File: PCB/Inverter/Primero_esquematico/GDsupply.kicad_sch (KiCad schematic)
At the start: 43 parts, among them T1 750317595, U1 UCC21750QDWRQ1, U2 LM25180QNGURQ1

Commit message: Correcciones incompletas e instalaciones de un par de extensiones copadas
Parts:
- removed C2, C3: 10uF, symbol Device:C
- removed C4: 47nF, symbol Device:C
- removed D1: 1N4148WS-Q, Diode_SMD:D_SOD-323F, symbol Device:D
- removed D2: DFLZ24Q-7, symbol Device:D_Zener
- removed D3, D41: VS-10MQ100NTRPBF, symbol Device:D_Schottky
- removed D5: BZT52C18-7-F, symbol Device:D_Zener
- removed D6: BZT52-B8V2_R1_00001, symbol Device:D_Zener
- removed R1: 307k, symbol Device:R
- removed R2: 37k, symbol Device:R
- removed R3: 12k1, symbol Device:R
- removed R4: 200k, symbol Device:R
- removed R5: 154k, symbol Device:R
- removed T1: 750317595, FSAE-footprints:WE-FLYTI_EP7_4436, symbol Fsae:750317595
- removed U2: LM25180QNGURQ1, NGU0008C, symbol Fsae:LM25180QNGURQ1
- added C2: EEH-ZS1H271UP, Capacitor_SMD:CP_Elec_10x10, symbol Device:C_Polarized_Small_US
- added D1: SMDJ13A, Diode_SMD:D_SMC, symbol Device:D_TVS
- added J1: IHL0212D1509, Snapeda:CONN5_05D1509_XPR, symbol Snapeda:IHL0205D1509
- added L1: MLZ2012N6R8LT000, Inductor_SMD:L_0805_2012Metric, symbol Device:L
- C1: value 10uF -> CL31B475KAHNNNE; footprint (none) -> Capacitor_SMD:C_1206_3216Metric; Compra (none) -> https://www.digikey.com/en/products/detail/samsung-electro-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
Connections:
- net +15V: now also J1.7 (+Vout)
- net -8V: now also J1.5 (-Vout)
- net GND: now also C1.2, C2.2, D1.2 (A2), J1.2 (-Vin); no longer C1.1
- net ISO_GND: now also J1.6 (Common)
- net Vin_FB: now also L1.1; no longer C1.2
- new net: C1.1, C2.1, D1.1 (A1), J1.1 (+Vin), L1.2
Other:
- note added: "Circuito basado en el LM25180-Q1 Se descarto este integrado por ocupar mucho espacio"
- note removed: "Circuito basado en el LM25180-Q1"
- note removed: "Recalcular en caso de usar otra fuente (En este caso se utilizaron fuente de 15V) Vin(on) = 14V Vin(off) = 12V"

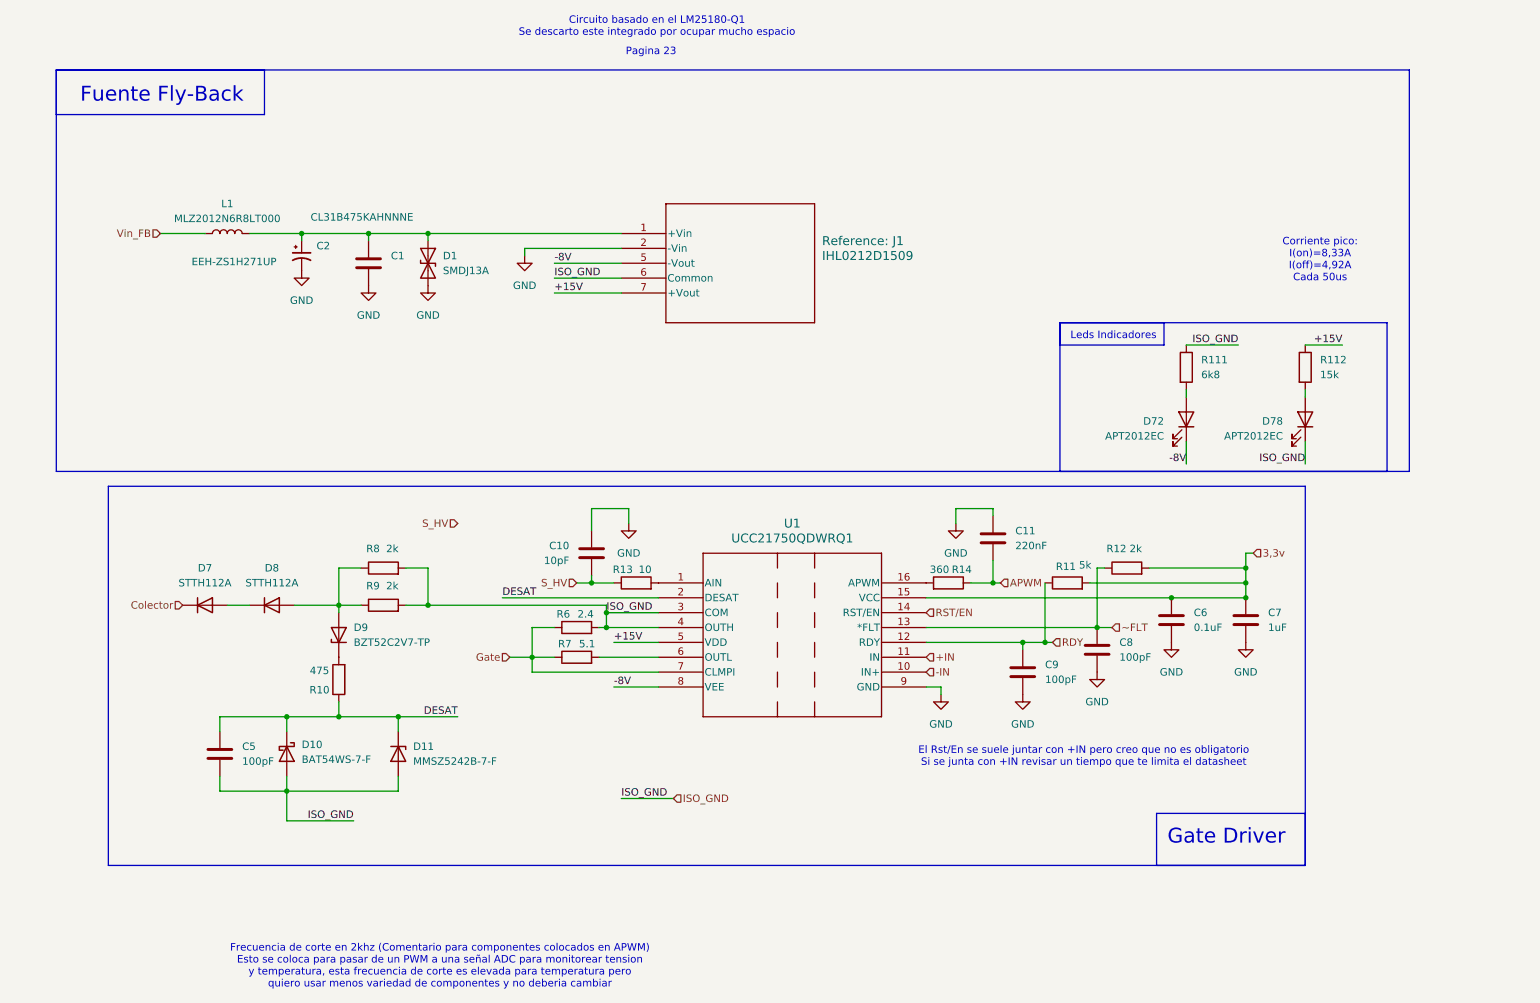
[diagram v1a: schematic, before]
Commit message: Coloque filtros y sensores
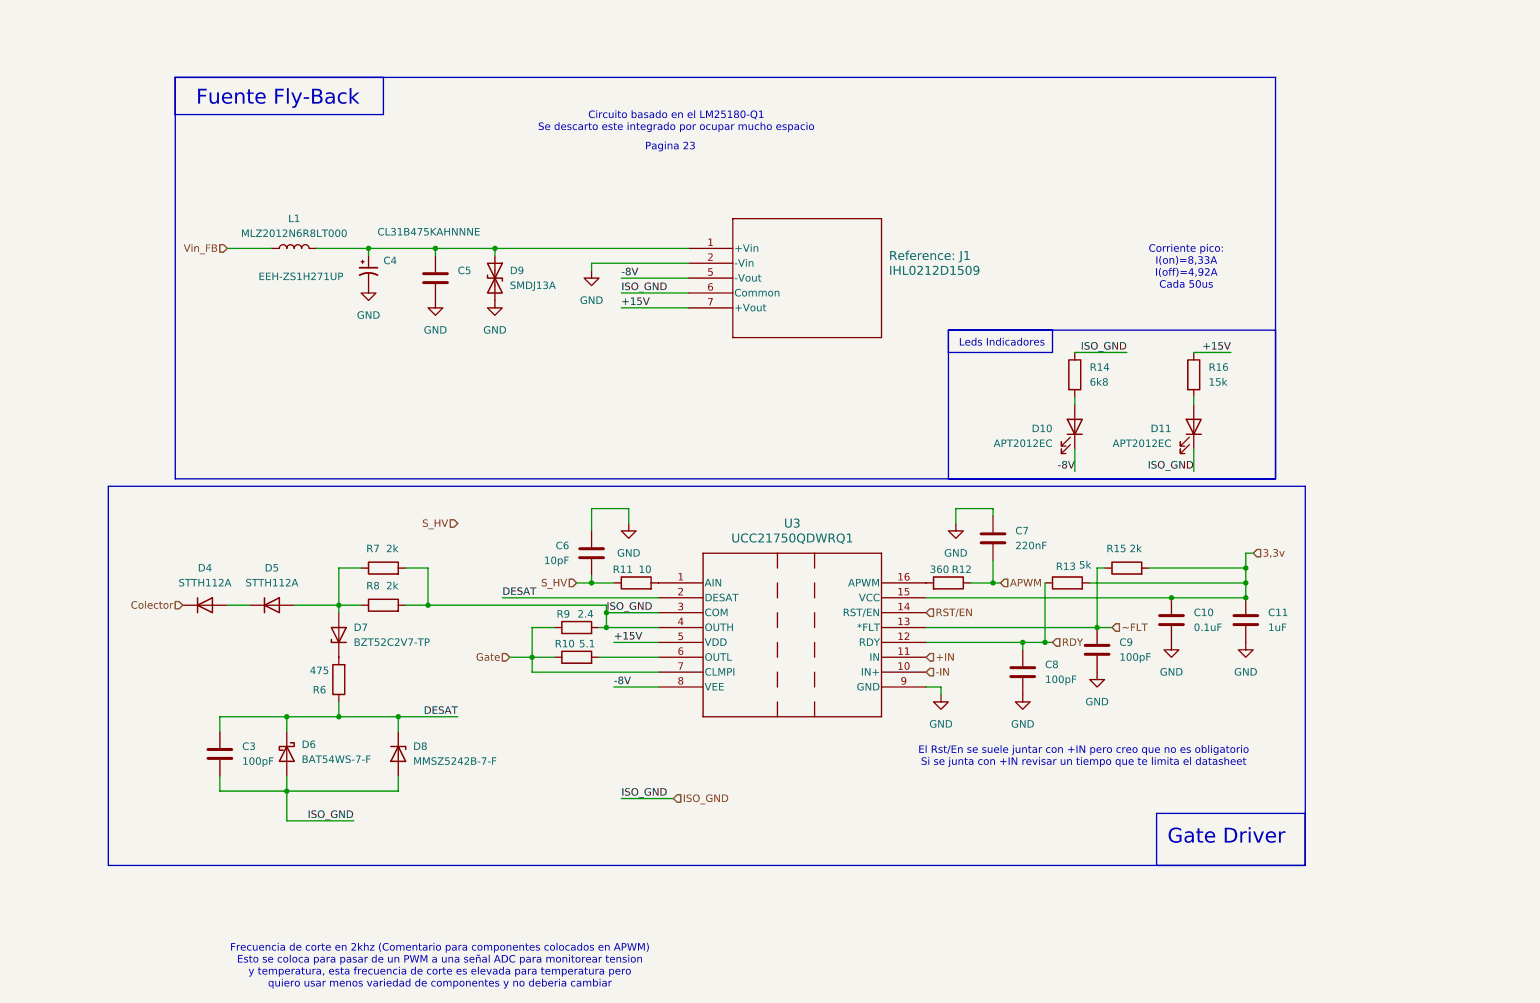
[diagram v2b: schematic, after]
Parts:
- renumbered C6 to C10, C7 to C11, C5 to C3, C2 to C4, C1 to C5, C10 to C6, C11 to C7, C9 to C8, C8 to C9, D72 to D10, D78 to D11, D7 to D4, D8 to D5, D10 to D6, D9 to D7, D11 to D8, D1 to D9, R7 to R10, R13 to R11, R14 to R12, R11 to R13, R111 to R14, R12 to R15, R112 to R16, R10 to R6, R8 to R7, R9 to R8, R6 to R9, U1 to U3
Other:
- moved on the sheet: C4, C5, D10, D11, D9, L1, R14, R16, Reference: J1

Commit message: Esquematico practicamente terminado
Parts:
- C39: renamed from C3; footprint (none) -> Capacitor_SMD:C_0402_1005Metric
- C42: renamed from C6; footprint (none) -> Capacitor_SMD:C_0402_1005Metric
- C43: renamed from C7; footprint (none) -> Capacitor_SMD:C_0603_1608Metric
- C44: renamed from C8; footprint (none) -> Capacitor_SMD:C_0402_1005Metric
- C45: renamed from C9; footprint (none) -> Capacitor_SMD:C_0402_1005Metric
- C46: renamed from C10; footprint (none) -> Capacitor_SMD:C_0603_1608Metric
- C47: renamed from C11; footprint (none) -> Capacitor_SMD:C_0603_1608Metric
- D38: renamed from D6; footprint (none) -> Diode_SMD:D_SOD-323_HandSoldering
- D42: renamed from D10; footprint (none) -> LED_SMD:LED_0805_2012Metric
- D43: renamed from D11; footprint (none) -> LED_SMD:LED_0805_2012Metric
- R50: renamed from R6; footprint (none) -> Resistor_SMD:R_0805_2012Metric
- R51: renamed from R7; footprint (none) -> Resistor_SMD:R_0805_2012Metric
- R52: renamed from R8; footprint (none) -> Resistor_SMD:R_0805_2012Metric
- R53: renamed from R9; footprint (none) -> Resistor_SMD:R_1206_3216Metric
- R54: renamed from R10; footprint (none) -> Resistor_SMD:R_1206_3216Metric
- R55: renamed from R11; footprint (none) -> Resistor_SMD:R_0402_1005Metric
- R56: renamed from R12; footprint (none) -> Resistor_SMD:R_0402_1005Metric
- R57: renamed from R13; footprint (none) -> Resistor_SMD:R_0402_1005Metric
- R58: renamed from R14; footprint (none) -> Resistor_SMD:R_0402_1005Metric
- R59: renamed from R15; footprint (none) -> Resistor_SMD:R_0805_2012Metric
- R60: renamed from R16; footprint (none) -> Resistor_SMD:R_0402_1005Metric
- renumbered C4 to C40, C5 to C41, D4 to D36, D5 to D37, D7 to D39, D8 to D40, D9 to D41, J1 to J5, L1 to L5, U3 to U7
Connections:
- net ISO_GND: now also C42.2
- net GND renamed GND1
- net GND1: no longer C42.2

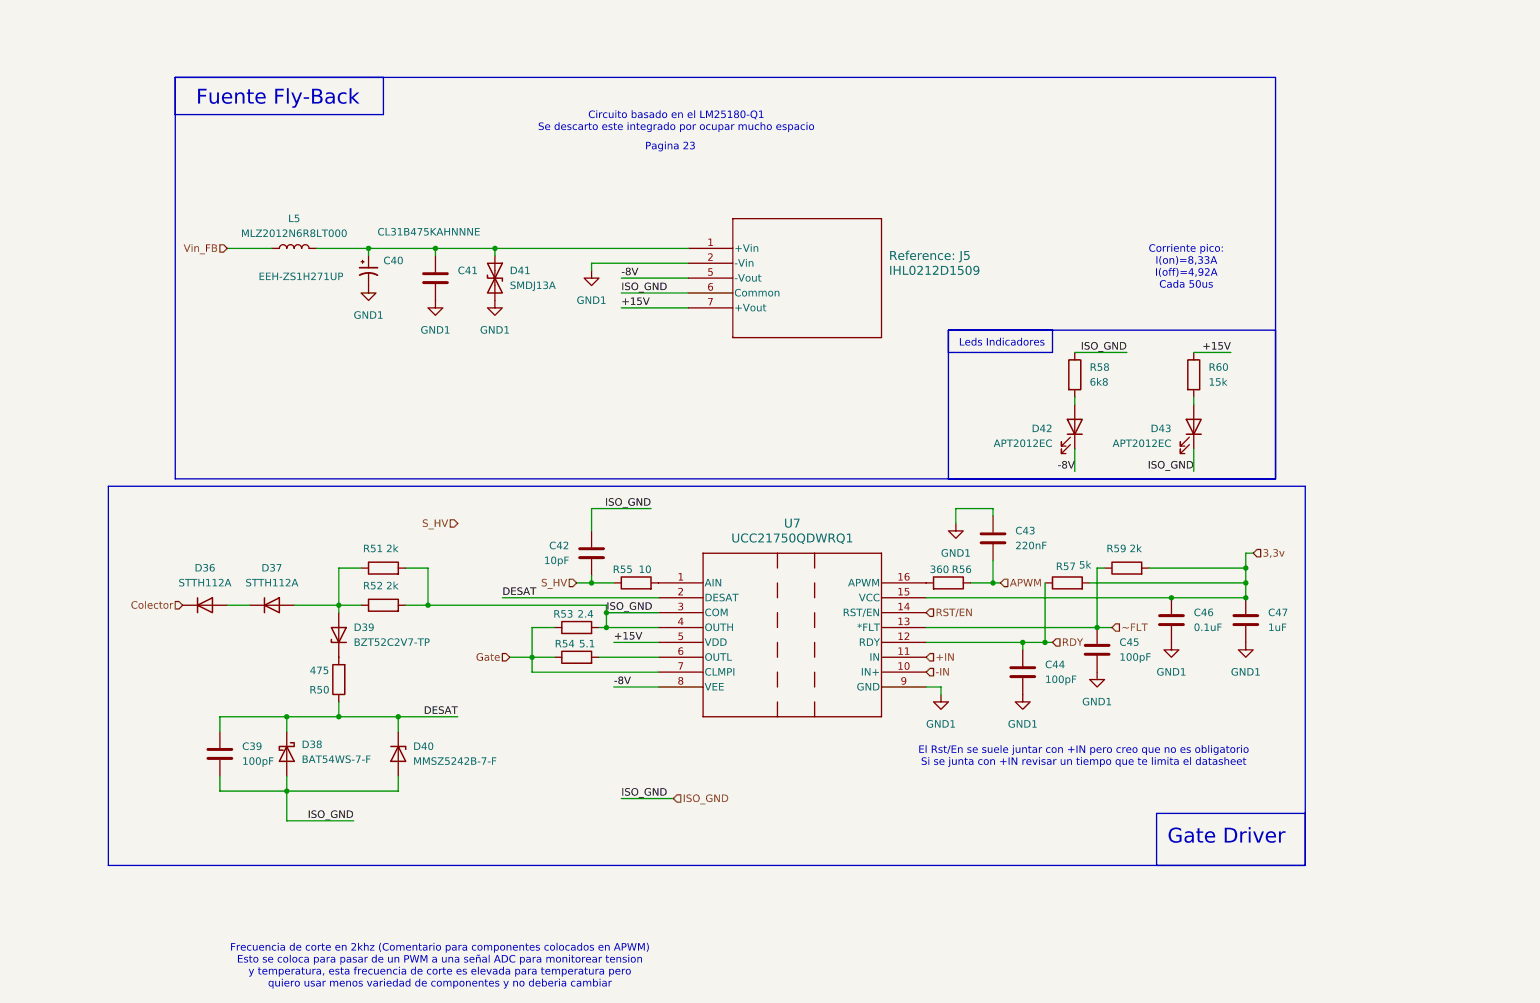
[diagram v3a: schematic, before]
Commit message: Un par de cosas q corregi del ERC pero sigue mal
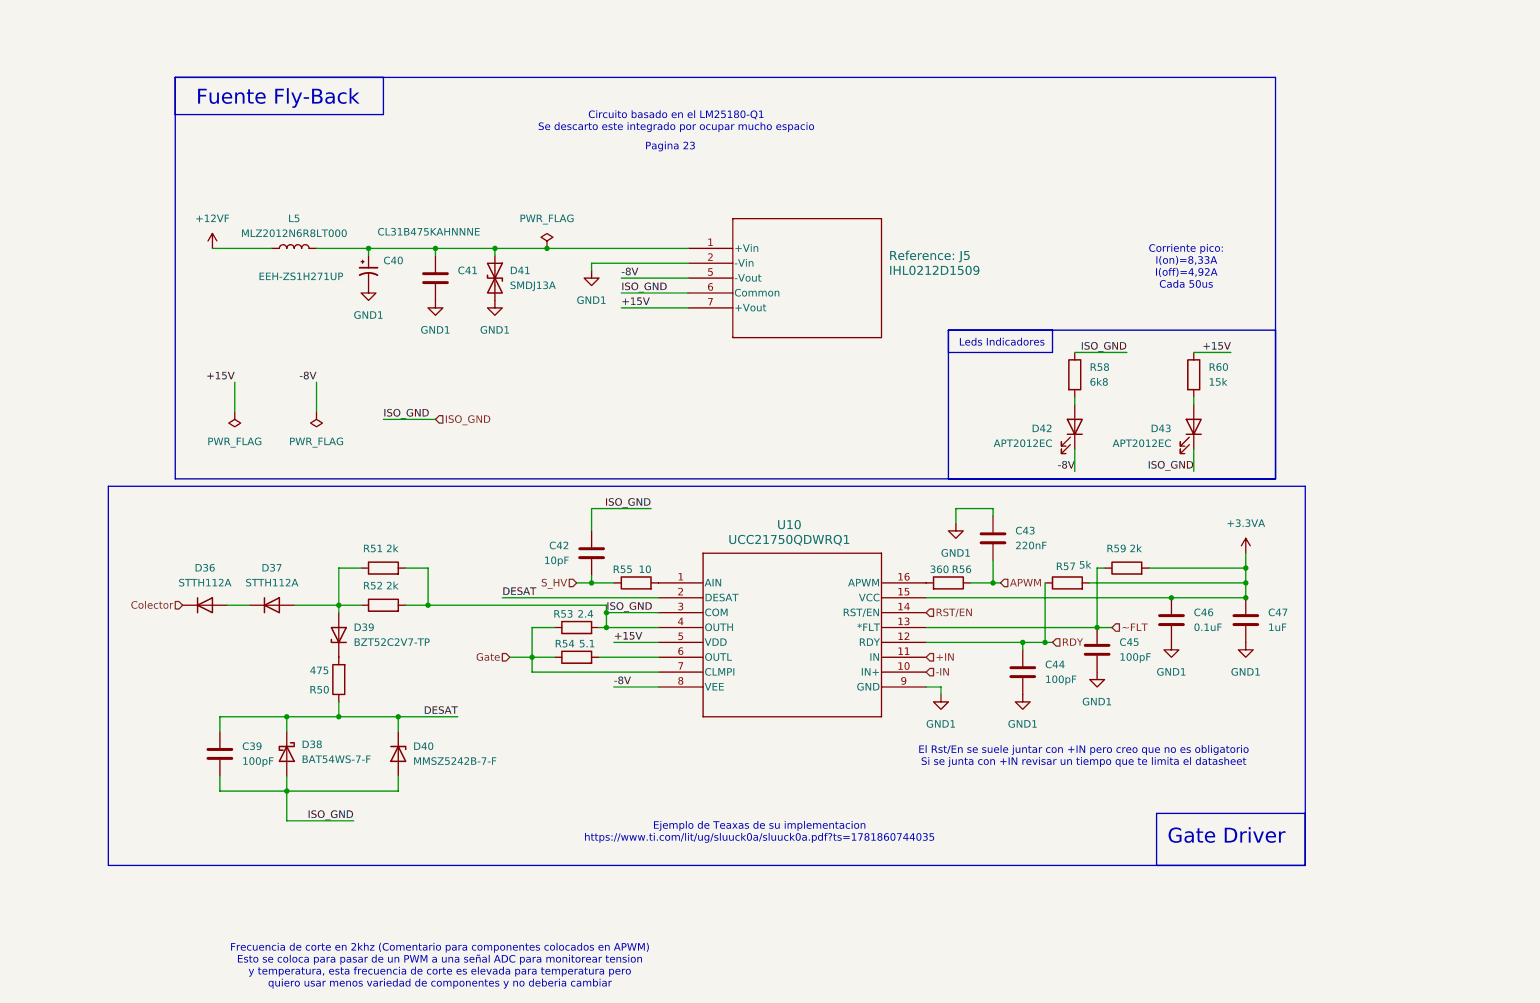
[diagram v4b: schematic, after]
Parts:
- removed U7: UCC21750QDWRQ1, SOIC16_DW_TEX, symbol FSAE-Simbols:UCC21750QDWRQ1
- added U10: UCC21750QDWRQ1, Snapeda:SOIC16_DW_TEX-L, symbol Snapeda:UCC21750QDWRQ1
- D39, D40: footprint (none) -> Diode_SMD:D_SOD-123
- J5: footprint Snapeda:CONN5_05D1509_XPR -> CONN5_05D1509_XPR
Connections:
- net +15V: now also U10.5 (VDD)
- net +IN: now also U10.11 (IN)
- net -8V: now also U10.8 (VEE)
- net -IN: now also U10.10 (IN+)
- net DESAT: now also U10.2 (DESAT)
- net GND1: now also U10.9 (GND)
- net Gate: now also U10.7 (CLMPI)
- net ISO_GND: now also U10.3 (COM), U10.4 (OUTH)
- net RDY: now also U10.12 (RDY)
- net RST/EN: now also U10.14 (RST/EN)
- net ~FLT: now also U10.13 (*FLT)
- net at R55.2: now also U10.1 (AIN)
- net at R56.2: now also U10.16 (APWM)
- net at R54.2: now also U10.6 (OUTL)
- net 3,3v renamed +3.3VA
- net +3.3VA: now also U10.15 (VCC)
- net Vin_FB renamed +12VF
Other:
- note added: "Ejemplo de Teaxas de su implementacion https://www.ti.com/lit/ug/sluuck0a/sluuck0a.pdf?ts=1781860744035"

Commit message: Esquematico Listo
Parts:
- C39: footprint Capacitor_SMD:C_0402_1005Metric -> Capacitor_SMD:C_0603_1608Metric_Pad1.08x0.95mm_HandSolder
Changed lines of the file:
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@@
 	)
 	(symbol
-		(lib_name "PWR_FLAG_3")
+		(lib_name "PWR_FLAG_1")
 		(lib_id "power:PWR_FLAG")
 		(at 76.2 82.55 180)
@@
 	)
 	(symbol
-		(lib_name "PWR_FLAG_1")
+		(lib_name "PWR_FLAG_3")
 		(lib_id "power:PWR_FLAG")
 		(at 115.57 54.61 0)
@@
 			)
 		)
-		(property "Footprint" "Capacitor_SMD:C_0402_1005Metric"
+		(property "Footprint" "Capacitor_SMD:C_0603_1608Metric_Pad1.08x0.95mm_HandSolder"
 			(at 58.7248 137.16 0)
 			(hide yes)

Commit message: Un par de cosas mas
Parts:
- removed C40: EEH-ZS1H271UP, Capacitor_SMD:CP_Elec_10x10, symbol Device:C_Polarized_Small_US
- removed C41: CL31B475KAHNNNE, Capacitor_SMD:C_1206_3216Metric, symbol Device:C
- removed D41: SMDJ13A, Diode_SMD:D_SMC, symbol Device:D_TVS
- removed D42, D43: APT2012EC, LED_SMD:LED_0805_2012Metric, symbol Device:LED
- removed J5: IHL0212D1509, CONN5_05D1509_XPR, symbol Snapeda:IHL0205D1509
- removed L5: MLZ2012N6R8LT000, Inductor_SMD:L_0805_2012Metric, symbol Device:L
- removed R58: 6k8, Resistor_SMD:R_0402_1005Metric, symbol Device:R
- removed R60: 15k, Resistor_SMD:R_0402_1005Metric, symbol Device:R
- added C123: 10 uF, Capacitor_SMD:C_1206_3216Metric, symbol Device:C
- added C124: 47nF, Capacitor_SMD:C_0402_1005Metric_Pad0.74x0.62mm_HandSolder, symbol Device:C
- added C125, C157: 10uF, Capacitor_SMD:C_0805_2012Metric, symbol Device:C
- added C141, C163: 22uF, Capacitor_SMD:C_0805_2012Metric, symbol Device:C
- added C151: 100nF, Capacitor_SMD:C_0402_1005Metric, symbol Device:C
- added D101, D68: SDM1U100S1F-7, Diode_SMD:D_SOD-123F, symbol Device:D_Schottky
- added D65: BZT52C18-7-F, Diode_SMD:D_SOD-123, symbol Device:D_Zener
- added D66: DFLZ24Q-7, Diode_SMD:D_PowerDI-123, symbol Device:D_Zener
- added D67: 1N4148WS-Q, Diode_SMD:D_SOD-323F, symbol Device:D
- added D83: BZT52B8V2-E3-08, Diode_SMD:D_SOD-123, symbol Device:D_Zener
- added R178: 246k, Resistor_SMD:R_0402_1005Metric, symbol Device:R
- added R196: 37k, Resistor_SMD:R_0402_1005Metric, symbol Device:R
- added R197: 12k1, Resistor_SMD:R_0402_1005Metric, symbol Device:R
- added R198: 110k, Resistor_SMD:R_0402_1005Metric, symbol Device:R
- added R199: 154k, Resistor_SMD:R_0402_1005Metric_Pad0.72x0.64mm_HandSolder, symbol Device:R
- added T1: 750317595, Snapeda:WE-FLYTI_EP7_4436, symbol Snapeda:750317595
- added TP53, TP59: TestPoint, TestPoint:TestPoint_Pad_D2.0mm, symbol Connector:TestPoint
- added U40: LM25180QNGURQ1, NGU0008C, symbol Snapeda:LM25180QNGURQ1
- C43: footprint Capacitor_SMD:C_0603_1608Metric -> Capacitor_SMD:C_0402_1005Metric
- R59: footprint Resistor_SMD:R_0805_2012Metric -> Resistor_SMD:R_0402_1005Metric
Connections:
- net +12VF: now also C123.1, C151.2, D66.2 (A), R178.1, T1.4, U40.3 (VIN)
- net +15V: now also C125.2, C157.2, D65.1 (K), D68.1 (K), TP53.1
- net -8V: now also C141.1, C163.1, D101.2 (A), D83.2 (A), TP59.1
- net ISO_GND: now also C125.1, C141.2, C157.1, C163.2, D65.2 (A), D83.1 (K), T1.6, T1.7
- new net: R178.2, R196.1, U40.4 (EN_UVLO)
- new net: R197.1, R198.1, U40.6 (TC)
- new net: R198.2, U40.7 (RSET)
- new net: D101.1 (K), T1.8
- new net: D67.2 (A), R199.1, T1.1, U40.1 (SW)
- new net: D68.2 (A), T1.5
- new net: C124.2, U40.5 (SS_BIAS)
- new net: D66.1 (K), D67.1 (K)
- new net: R199.2, U40.2 (FB)
- new net GND: C123.2, C124.1, C151.1, R196.2, R197.2, U40.8 (GND), U40.9 (PAD)
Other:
- note added: "C_local >> Q_g/DeltaV"
- note added: "Circuito basado en el LM25180-Q1"
- note added: "Recalcular en caso de usar otra fuente (En este caso se utilizaron fuente de 15V) Vin(on) = 14V Vin(off) = 12V"
- note removed: "Circuito basado en el LM25180-Q1 Se descarto este integrado por ocupar mucho espacio"
- note removed: "Leds Indicadores"
- moved on the sheet: D39

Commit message: Sigo con la placa padre
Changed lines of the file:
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@@
-	)
-	(junction
-		(at 209.55 59.69)
-		(diameter 0)
-		(color 0 0 0 0)
 	)
 	(junction
@@
 		)
 		(stroke
-			(width 0)
-			(type default)
-		)
-	)
-	(wire
-		(pts
-			(xy 209.55 58.42) (xy 209.55 59.69)
-		)
-		(stroke
